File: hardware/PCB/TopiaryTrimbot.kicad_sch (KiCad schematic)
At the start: 0 parts

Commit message: LCD: working on video mode operation, KiCAD sheets
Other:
- added sheet LCD (lcd.kicad_sch)
- added sheet MCU (mcu.kicad_sch)
- added sheet Motor Control (motor.kicad_sch)
- added sheet Power (power.kicad_sch)
- added sheet Raspberry Pi (rpi.kicad_sch)
- added sheet Storage (storage.kicad_sch)
- note added: "Top-level Topiary Trimbot Schematic"

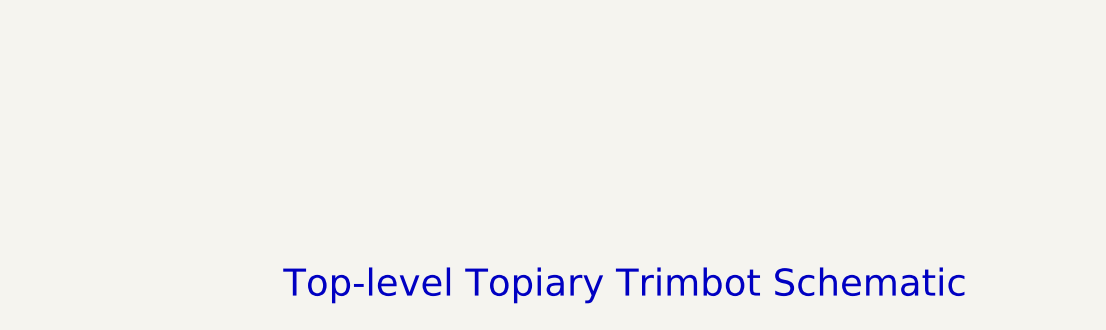
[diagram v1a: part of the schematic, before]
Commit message: LCD: Add in backlight driver, finish wiring
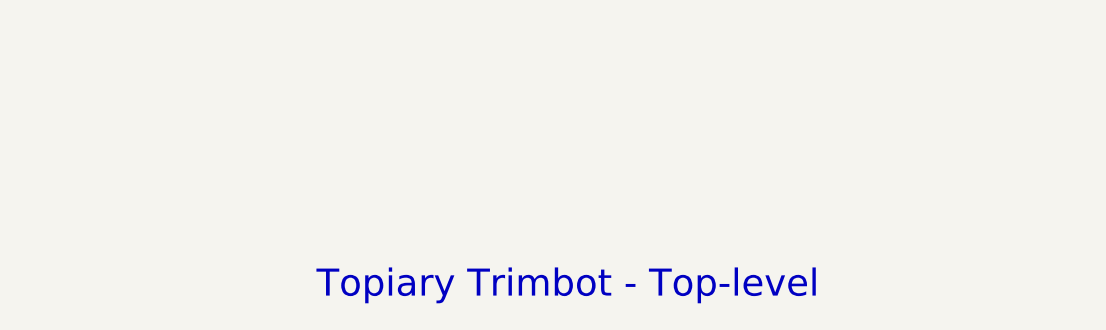
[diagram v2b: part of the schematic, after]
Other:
- note added: "Topiary Trimbot - Top-level"
- note removed: "Top-level Topiary Trimbot Schematic"
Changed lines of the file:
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@@
 	(generator_version "9.0")
 	(paper "A4")
-	(text "Top-level Topiary Trimbot Schematic"
+	(text "Topiary Trimbot - Top-level"
 		(exclude_from_sim no)
-		(at 220.98 173.99 0)
+		(at 214.63 173.99 0)
 		(effects
 			(font

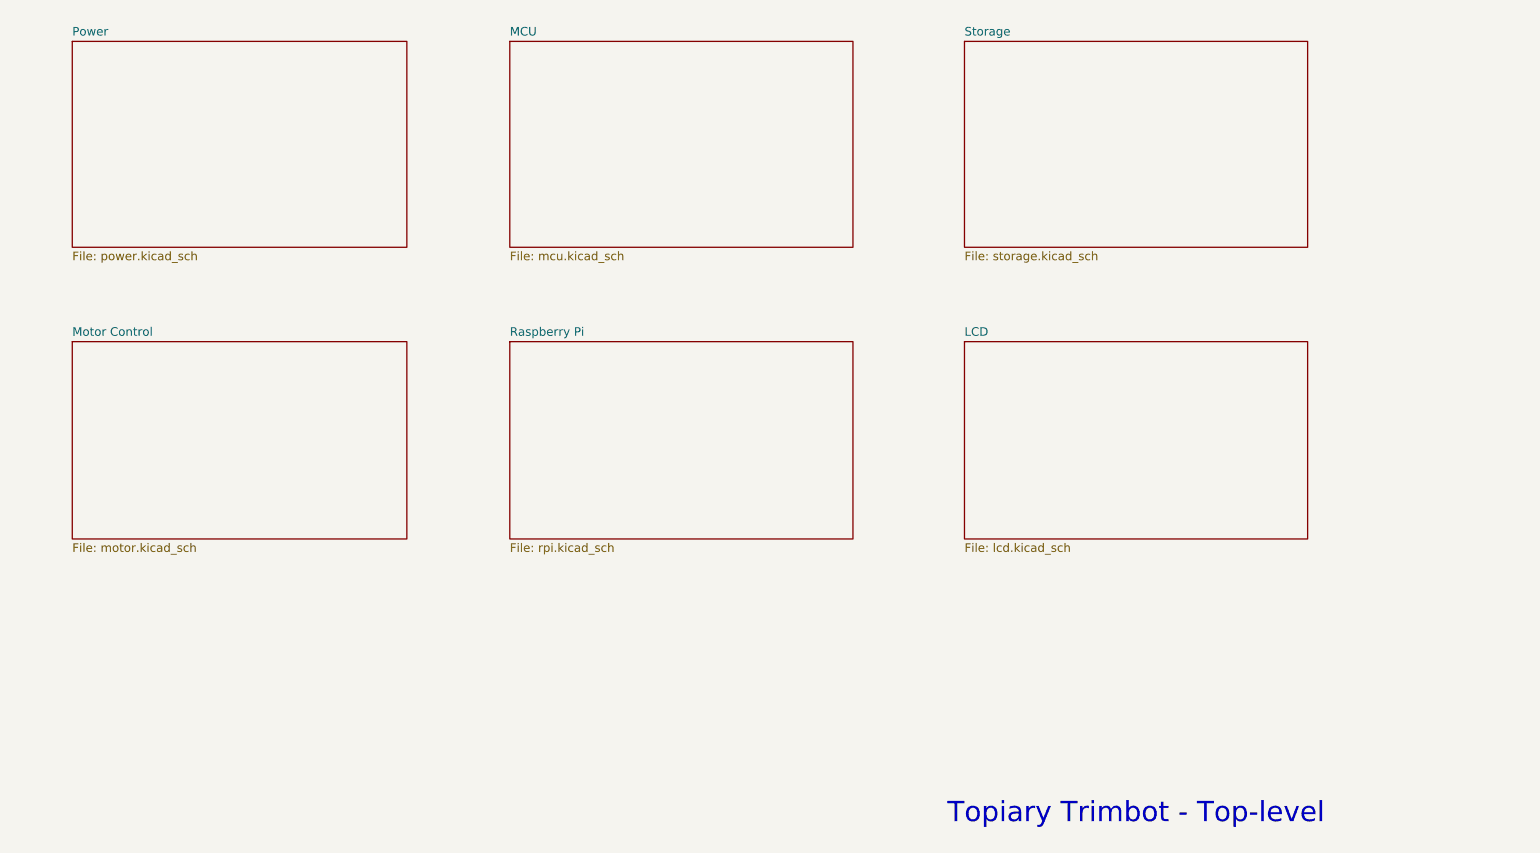
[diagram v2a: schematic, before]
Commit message: Schematic: Clearer top-level labels
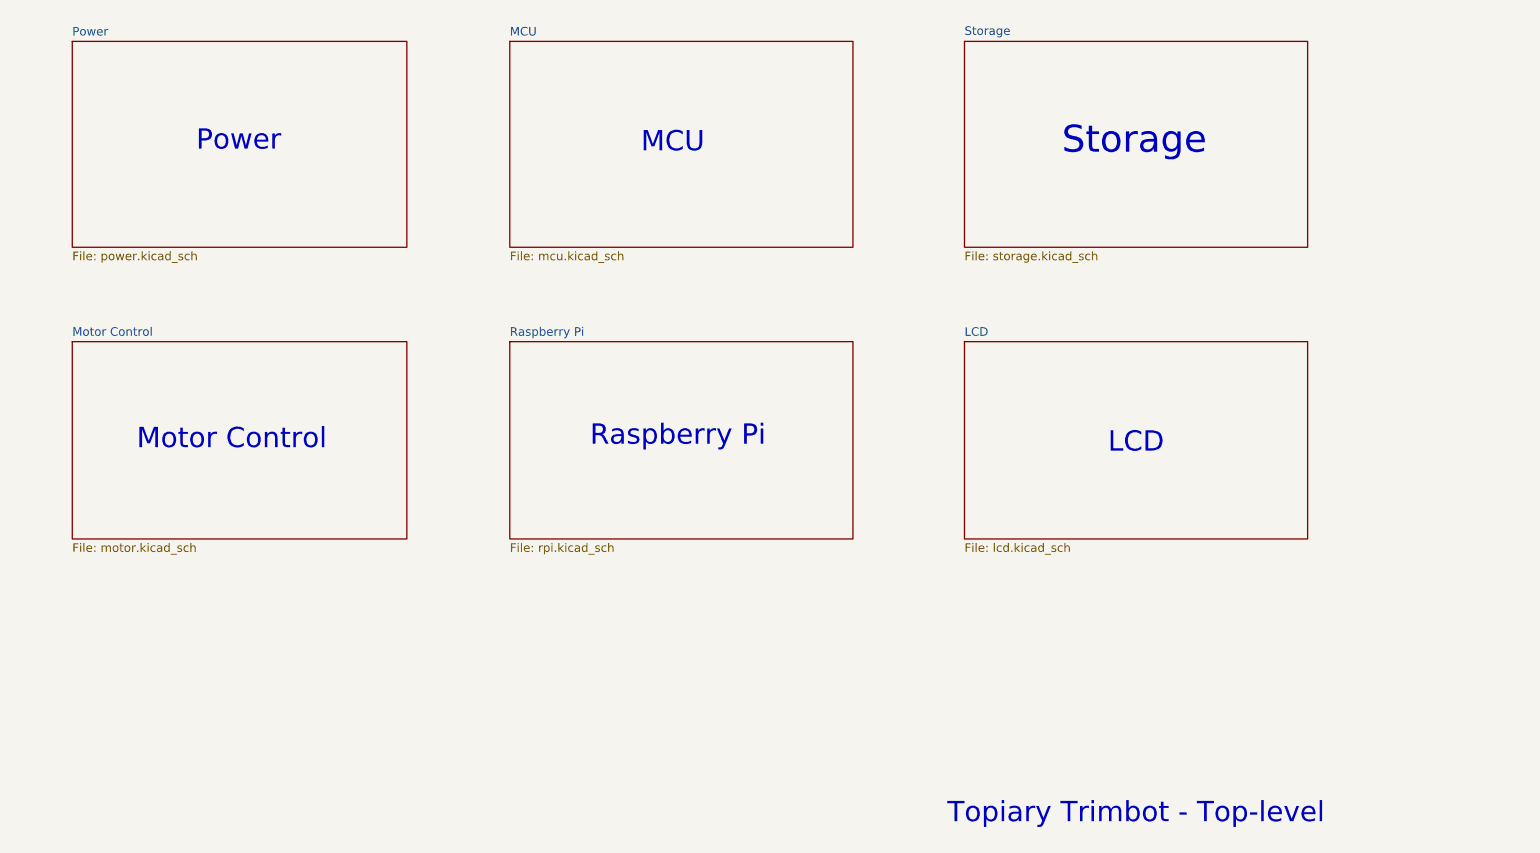
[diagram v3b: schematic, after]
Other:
- note added: "LCD"
- note added: "MCU"
- note added: "Motor Control"
- note added: "Power"
- note added: "Raspberry Pi"
- note added: "Storage"
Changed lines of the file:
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@@
 	(generator_version "9.0")
 	(paper "A4")
+	(text "Raspberry Pi"
+		(exclude_from_sim no)
+		(at 146.812 118.11 0)
+		(effects
+			(font
+				(size 3 3)
+			)
+		)
+	)
+	(text "Power"
+		(exclude_from_sim no)
+		(at 81.788 74.422 0)
+		(effects
+			(font
+				(size 3 3)
+			)
+		)
+	)
+	(text "Storage"
+		(exclude_from_sim no)
+		(at 214.376 74.422 0)
+		(effects
+			(font
+				(size 4 4)
+			)
+		)
+	)
+	(text "Motor Control"
+		(exclude_from_sim no)
+		(at 80.772 118.618 0)
+		(effects
+			(font
+				(size 3 3)
+			)
+		)
+	)
+	(text "MCU"
+		(exclude_from_sim no)
+		(at 146.05 74.676 0)
+		(effects
+			(font
+				(size 3 3)
+			)
+		)
+	)
+	(text "LCD"
+		(exclude_from_sim no)
+		(at 214.63 119.126 0)
+		(effects
+			(font
+				(size 3 3)
+			)
+		)
+	)
 	(text "Topiary Trimbot - Top-level"
 		(exclude_from_sim no)
@@
 		(on_board yes)
 		(dnp no)
-		(fields_autoplaced yes)
 		(stroke
 			(width 0.1524)
@@
 		)
 		(property "Sheetname" "Storage"
-			(at 189.23 58.9784 0)
+			(at 189.23 57.404 0)
 			(effects
 				(font
 					(size 1.27 1.27)
 				)
-				(justify left bottom)
+				(justify left top)
 			)
 		)

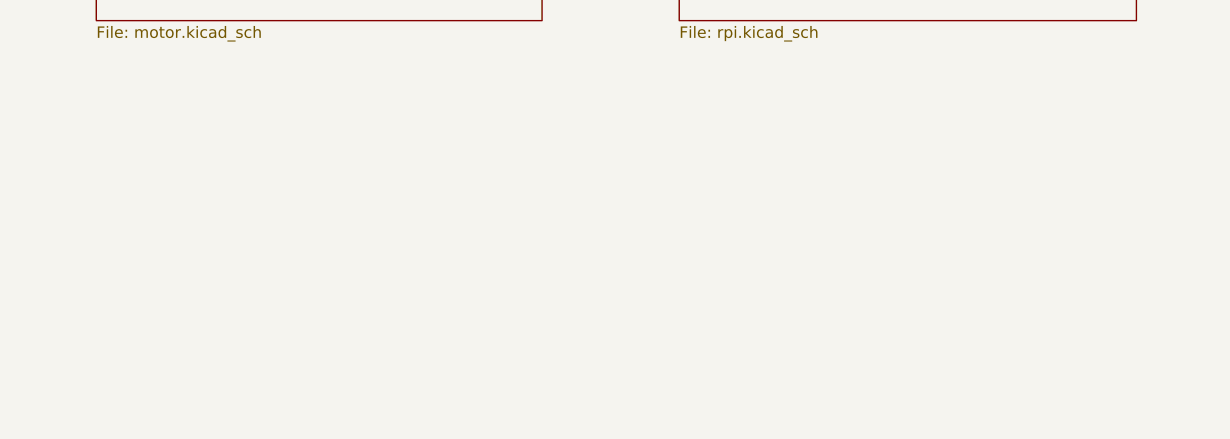
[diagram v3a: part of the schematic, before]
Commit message: mcu and top level update
more caps and mounting holes
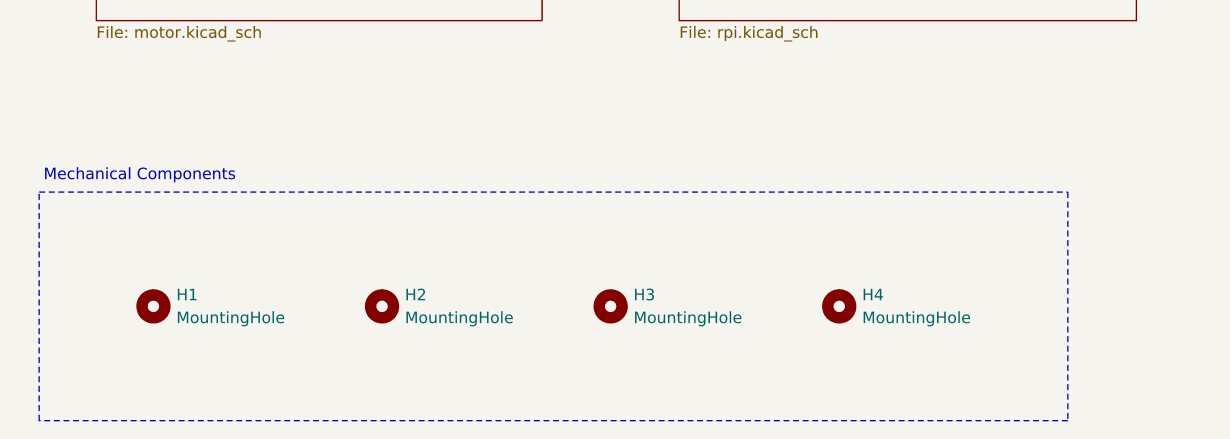
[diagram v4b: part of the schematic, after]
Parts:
- added H1, H2, H3, H4: MountingHole, symbol Mechanical:MountingHole
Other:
- note added: "Mechanical Components"

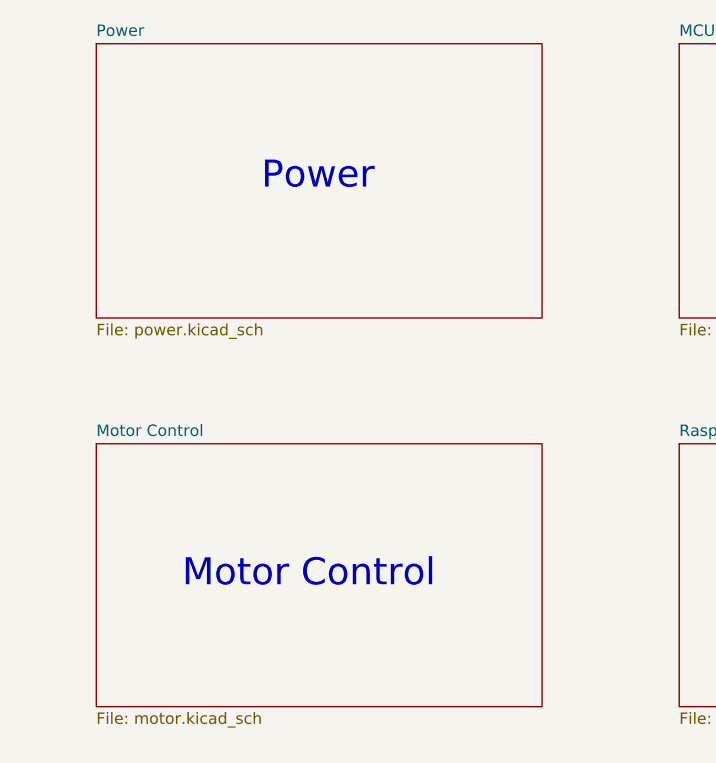
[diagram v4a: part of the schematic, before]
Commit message: Finished setting footprints for LCD, motors, RPi, and storage schematics
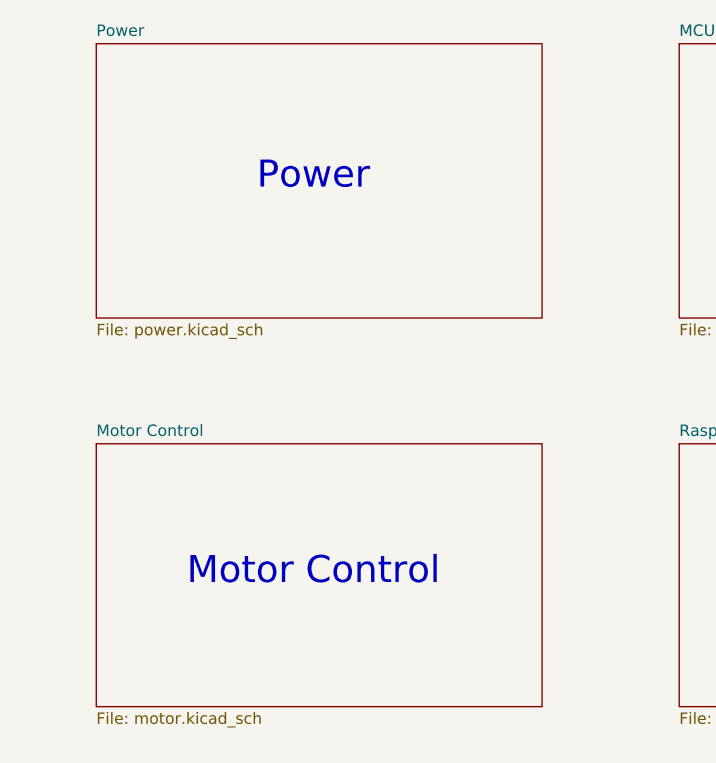
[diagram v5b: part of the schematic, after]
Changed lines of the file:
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@@
 	(text "Power"
 		(exclude_from_sim no)
-		(at 81.788 74.422 0)
+		(at 81.28 74.422 0)
 		(effects
 			(font
@@
 	(text "Motor Control"
 		(exclude_from_sim no)
-		(at 80.772 118.618 0)
+		(at 81.28 118.364 0)
 		(effects
 			(font

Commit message: Touch up some ERC violations
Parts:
- H1, H2, H3, H4: footprint (none) -> MountingHole:MountingHole_3.2mm_M3_Pad_TopBottom
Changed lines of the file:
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@@
 			)
 		)
-		(property "Footprint" ""
+		(property "Footprint" "MountingHole:MountingHole_3.2mm_M3_Pad_TopBottom"
 			(at 139.7 165.1 0)
 			(effects
@@
 			)
 		)
-		(property "Footprint" ""
+		(property "Footprint" "MountingHole:MountingHole_3.2mm_M3_Pad_TopBottom"
 			(at 114.3 165.1 0)
 			(effects
@@
 			)
 		)
-		(property "Footprint" ""
+		(property "Footprint" "MountingHole:MountingHole_3.2mm_M3_Pad_TopBottom"
 			(at 63.5 165.1 0)
 			(effects
@@
 			)
 		)
-		(property "Footprint" ""
+		(property "Footprint" "MountingHole:MountingHole_3.2mm_M3_Pad_TopBottom"
 			(at 88.9 165.1 0)
 			(effects
